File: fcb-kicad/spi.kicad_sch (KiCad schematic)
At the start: 12 parts, among them J3 Conn_Coaxial, U4 W25Q128JVS, U5 LSM6DS3, U6 DL-RTS4432

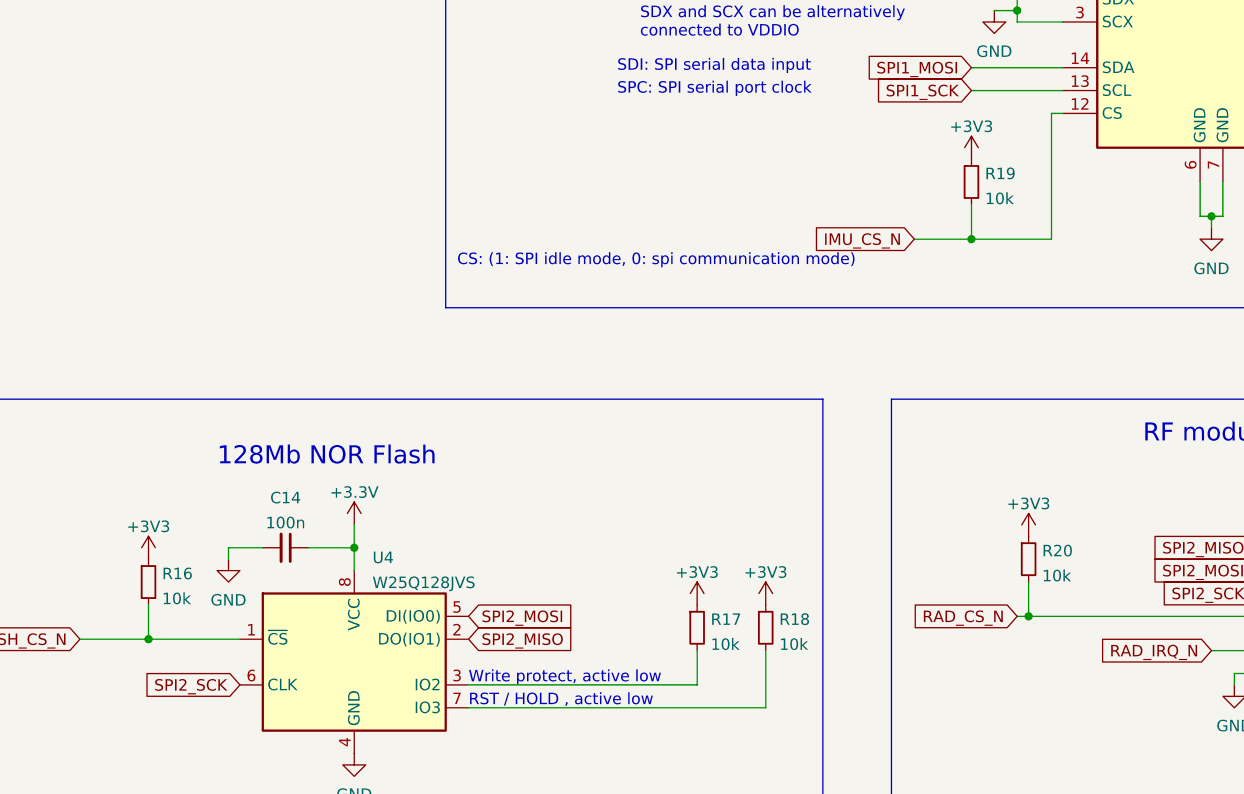
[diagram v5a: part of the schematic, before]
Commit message: Less routing on inner layers, fabrication, BOM should be OK
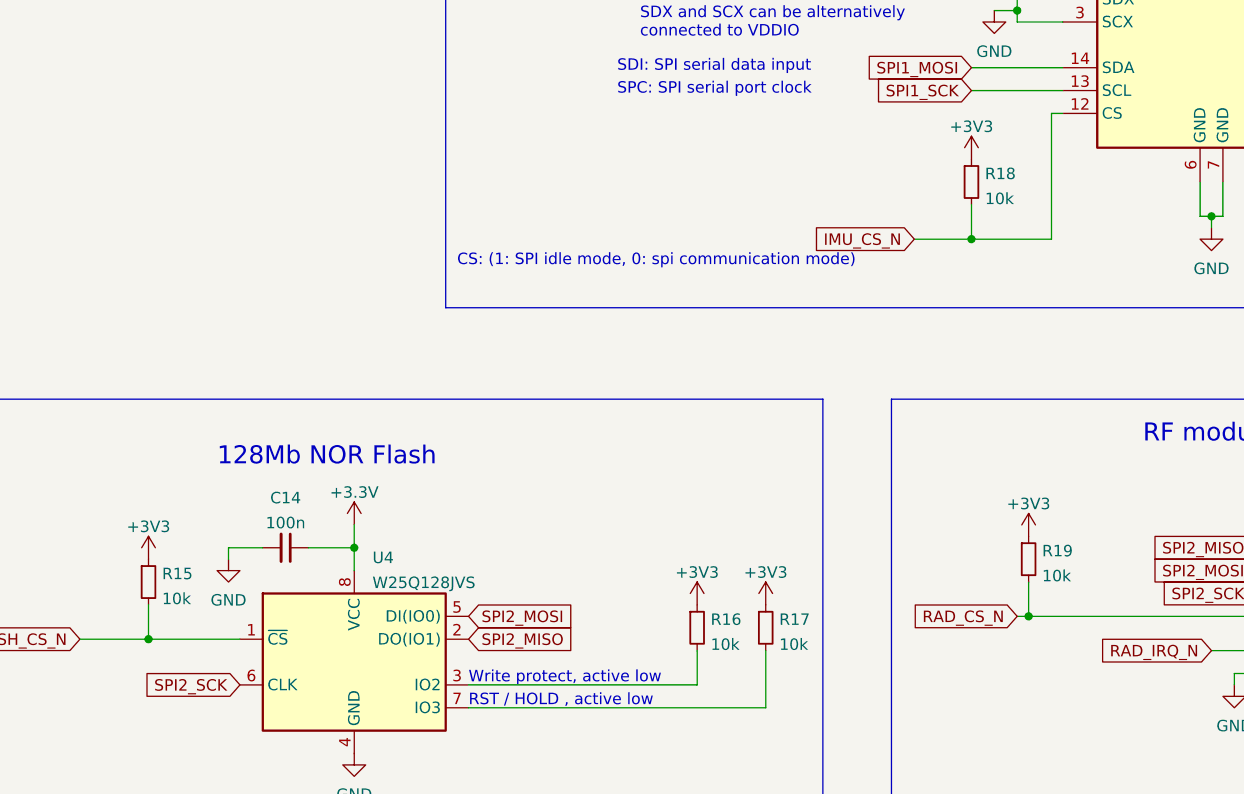
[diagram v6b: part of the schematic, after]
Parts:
- R15: renamed from R16; LCSC (none) -> C25804
- R16: renamed from R17; LCSC (none) -> C25804
- R17: renamed from R18; LCSC (none) -> C25804
- R18: renamed from R19; LCSC (none) -> C25804
- R19: renamed from R20; LCSC (none) -> C25804
- U4: LCSC (none) -> C97521
- U5: LCSC (none) -> C95230
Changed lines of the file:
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@@
   (symbol (lib_id "Device:R_Small") (at 168.91 80.01 0) (unit 1)
     (in_bom yes) (on_board yes) (fields_autoplaced)
-    (property "Reference" "R19" (id 0) (at 170.4086 79.1015 0)
+    (property "Reference" "R18" (id 0) (at 170.4086 79.1015 0)
       (effects (font (size 1.27 1.27)) (justify left))
     )
@@
       (effects (font (size 1.27 1.27)) hide)
     )
+    (property "LCSC" "C25804" (id 4) (at 168.91 80.01 0)
+      (effects (font (size 1.27 1.27)) hide)
+    )
     (pin "1")
     (pin "2")
@@
   (symbol (lib_id "power:+3V3") (at 194.31 45.72 0) (unit 1)
     (in_bom yes) (on_board yes)
-    (property "Reference" "#PWR044" (id 0) (at 194.31 49.53 0)
+    (property "Reference" "#PWR043" (id 0) (at 194.31 49.53 0)
       (effects (font (size 1.27 1.27)) hide)
     )
@@
   (symbol (lib_id "power:+3V3") (at 168.91 77.47 0) (unit 1)
     (in_bom yes) (on_board yes)
-    (property "Reference" "#PWR041" (id 0) (at 168.91 81.28 0)
+    (property "Reference" "#PWR040" (id 0) (at 168.91 81.28 0)
       (effects (font (size 1.27 1.27)) hide)
     )
@@
   (symbol (lib_id "Device:R_Small") (at 77.47 124.46 0) (unit 1)
     (in_bom yes) (on_board yes) (fields_autoplaced)
-    (property "Reference" "R16" (id 0) (at 78.9686 123.5515 0)
+    (property "Reference" "R15" (id 0) (at 78.9686 123.5515 0)
       (effects (font (size 1.27 1.27)) (justify left))
     )
@@
       (effects (font (size 1.27 1.27)) hide)
     )
+    (property "LCSC" "C25804" (id 4) (at 77.47 124.46 0)
+      (effects (font (size 1.27 1.27)) hide)
+    )
     (pin "1")
     (pin "2")
@@
   (symbol (lib_id "power:GND") (at 210.82 146.05 0) (unit 1)
     (in_bom yes) (on_board yes) (fields_autoplaced)
-    (property "Reference" "#PWR048" (id 0) (at 210.82 152.4 0)
+    (property "Reference" "#PWR047" (id 0) (at 210.82 152.4 0)
       (effects (font (size 1.27 1.27)) hide)
     )
@@
   (symbol (lib_id "power:GND") (at 234.95 83.82 0) (unit 1)
     (in_bom yes) (on_board yes) (fields_autoplaced)
-    (property "Reference" "#PWR052" (id 0) (at 234.95 90.17 0)
+    (property "Reference" "#PWR051" (id 0) (at 234.95 90.17 0)
       (effects (font (size 1.27 1.27)) hide)
     )
@@
   (symbol (lib_id "power:+3.3V") (at 210.82 115.57 0) (unit 1)
     (in_bom yes) (on_board yes) (fields_autoplaced)
-    (property "Reference" "#PWR047" (id 0) (at 210.82 119.38 0)
+    (property "Reference" "#PWR046" (id 0) (at 210.82 119.38 0)
       (effects (font (size 1.27 1.27)) hide)
     )
@@
   (symbol (lib_id "power:+3.3V") (at 100.33 118.11 0) (unit 1)
     (in_bom yes) (on_board yes) (fields_autoplaced)
-    (property "Reference" "#PWR037" (id 0) (at 100.33 121.92 0)
+    (property "Reference" "#PWR036" (id 0) (at 100.33 121.92 0)
       (effects (font (size 1.27 1.27)) hide)
     )
@@
   (symbol (lib_id "Device:R_Small") (at 175.26 121.92 0) (unit 1)
     (in_bom yes) (on_board yes) (fields_autoplaced)
-    (property "Reference" "R20" (id 0) (at 176.7586 121.0115 0)
+    (property "Reference" "R19" (id 0) (at 176.7586 121.0115 0)
       (effects (font (size 1.27 1.27)) (justify left))
     )
@@
       (effects (font (size 1.27 1.27)) hide)
     )
+    (property "LCSC" "C25804" (id 4) (at 175.26 121.92 0)
+      (effects (font (size 1.27 1.27)) hide)
+    )
     (pin "1")
     (pin "2")
@@
   (symbol (lib_id "power:+3V3") (at 224.79 72.39 0) (unit 1)
     (in_bom yes) (on_board yes)
-    (property "Reference" "#PWR049" (id 0) (at 224.79 76.2 0)
+    (property "Reference" "#PWR048" (id 0) (at 224.79 76.2 0)
       (effects (font (size 1.27 1.27)) hide)
     )
@@
   (symbol (lib_id "power:+3V3") (at 77.47 121.92 0) (unit 1)
     (in_bom yes) (on_board yes)
-    (property "Reference" "#PWR035" (id 0) (at 77.47 125.73 0)
+    (property "Reference" "#PWR034" (id 0) (at 77.47 125.73 0)
       (effects (font (size 1.27 1.27)) hide)
     )
@@
   (symbol (lib_id "power:+3V3") (at 138.43 127 0) (unit 1)
     (in_bom yes) (on_board yes)
-    (property "Reference" "#PWR039" (id 0) (at 138.43 130.81 0)
+    (property "Reference" "#PWR038" (id 0) (at 138.43 130.81 0)
       (effects (font (size 1.27 1.27)) hide)
     )
@@
   (symbol (lib_id "Device:R_Small") (at 146.05 129.54 0) (unit 1)
     (in_bom yes) (on_board yes) (fields_autoplaced)
-    (property "Reference" "R18" (id 0) (at 147.5486 128.6315 0)
+    (property "Reference" "R17" (id 0) (at 147.5486 128.6315 0)
       (effects (font (size 1.27 1.27)) (justify left))
     )
@@
       (effects (font (size 1.27 1.27)) hide)
     )
+    (property "LCSC" "C25804" (id 4) (at 146.05 129.54 0)
+      (effects (font (size 1.27 1.27)) hide)
+    )
     (pin "1")
     (pin "2")
@@
   (symbol (lib_id "power:GND") (at 224.79 83.82 0) (unit 1)
     (in_bom yes) (on_board yes) (fields_autoplaced)
-    (property "Reference" "#PWR050" (id 0) (at 224.79 90.17 0)
+    (property "Reference" "#PWR049" (id 0) (at 224.79 90.17 0)
       (effects (font (size 1.27 1.27)) hide)
     )
@@
   (symbol (lib_id "power:GND") (at 195.58 85.09 0) (unit 1)
     (in_bom yes) (on_board yes) (fields_autoplaced)
-    (property "Reference" "#PWR045" (id 0) (at 195.58 91.44 0)
+    (property "Reference" "#PWR044" (id 0) (at 195.58 91.44 0)
       (effects (font (size 1.27 1.27)) hide)
     )
@@
   (symbol (lib_id "power:GND") (at 241.3 129.54 0) (unit 1)
     (in_bom yes) (on_board yes) (fields_autoplaced)
-    (property "Reference" "#PWR053" (id 0) (at 241.3 135.89 0)
+    (property "Reference" "#PWR052" (id 0) (at 241.3 135.89 0)
       (effects (font (size 1.27 1.27)) hide)
     )
@@
   (symbol (lib_id "power:+3V3") (at 175.26 119.38 0) (unit 1)
     (in_bom yes) (on_board yes)
-    (property "Reference" "#PWR043" (id 0) (at 175.26 123.19 0)
+    (property "Reference" "#PWR042" (id 0) (at 175.26 123.19 0)
       (effects (font (size 1.27 1.27)) hide)
     )
@@
   (symbol (lib_id "power:+3V3") (at 234.95 72.39 0) (unit 1)
     (in_bom yes) (on_board yes)
-    (property "Reference" "#PWR051" (id 0) (at 234.95 76.2 0)
+    (property "Reference" "#PWR050" (id 0) (at 234.95 76.2 0)
       (effects (font (size 1.27 1.27)) hide)
     )
@@
     )
     (property "Datasheet" "http://www.winbond.com/resource-files/w25q128jv_dtr%20revc%2003272018%20plus.pdf" (id 3) (at 100.33 133.35 0)
+      (effects (font (size 1.27 1.27)) hide)
+    )
+    (property "LCSC" "C97521" (id 4) (at 100.33 133.35 0)
       (effects (font (size 1.27 1.27)) hide)
     )
@@
   (symbol (lib_id "Device:R_Small") (at 138.43 129.54 0) (unit 1)
     (in_bom yes) (on_board yes) (fields_autoplaced)
-    (property "Reference" "R17" (id 0) (at 139.9286 128.6315 0)
+    (property "Reference" "R16" (id 0) (at 139.9286 128.6315 0)
       (effects (font (size 1.27 1.27)) (justify left))
     )
@@
       (effects (font (size 1.27 1.27)) hide)
     )
+    (property "LCSC" "C25804" (id 4) (at 138.43 129.54 0)
+      (effects (font (size 1.27 1.27)) hide)
+    )
     (pin "1")
     (pin "2")
@@
   (symbol (lib_id "power:GND") (at 86.36 121.92 0) (unit 1)
     (in_bom yes) (on_board yes) (fields_autoplaced)
-    (property "Reference" "#PWR036" (id 0) (at 86.36 128.27 0)
+    (property "Reference" "#PWR035" (id 0) (at 86.36 128.27 0)
       (effects (font (size 1.27 1.27)) hide)
     )
@@
   (symbol (lib_id "power:GND") (at 100.33 143.51 0) (unit 1)
     (in_bom yes) (on_board yes) (fields_autoplaced)
-    (property "Reference" "#PWR038" (id 0) (at 100.33 149.86 0)
+    (property "Reference" "#PWR037" (id 0) (at 100.33 149.86 0)
       (effects (font (size 1.27 1.27)) hide)
     )
@@
     )
     (property "Datasheet" "https://content.arduino.cc/assets/st_imu_lsm6ds3_datasheet.pdf" (id 3) (at 196.85 81.28 0)
+      (effects (font (size 1.27 1.27)) hide)
+    )
+    (property "LCSC" "C95230" (id 4) (at 194.31 64.77 0)
       (effects (font (size 1.27 1.27)) hide)
     )
@@
   (symbol (lib_id "power:GND") (at 171.45 60.96 0) (unit 1)
     (in_bom yes) (on_board yes) (fields_autoplaced)
-    (property "Reference" "#PWR042" (id 0) (at 171.45 67.31 0)
+    (property "Reference" "#PWR041" (id 0) (at 171.45 67.31 0)
       (effects (font (size 1.27 1.27)) hide)
     )
@@
   (symbol (lib_id "power:GND") (at 198.12 135.89 0) (unit 1)
     (in_bom yes) (on_board yes) (fields_autoplaced)
-    (property "Reference" "#PWR046" (id 0) (at 198.12 142.24 0)
+    (property "Reference" "#PWR045" (id 0) (at 198.12 142.24 0)
       (effects (font (size 1.27 1.27)) hide)
     )
@@
   (symbol (lib_id "power:+3V3") (at 146.05 127 0) (unit 1)
     (in_bom yes) (on_board yes)
-    (property "Reference" "#PWR040" (id 0) (at 146.05 130.81 0)
-      (effects (font (size 1.27 1.27)) hide)
-    )
+    (property "Reference" "#PWR039" (id 0) (at 146.05 130.81 0)
+      (effects (font (size 1.27 1.27)) hide)
+    )
